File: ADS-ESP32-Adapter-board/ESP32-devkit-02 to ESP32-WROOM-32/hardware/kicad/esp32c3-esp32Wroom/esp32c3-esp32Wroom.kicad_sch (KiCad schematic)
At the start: 4 parts, among them J1 Conn_01x15_esp32_devkit_V1_el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, J2 Conn_01x15_esp32_devkit_V1_el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, J3 Conn_01x15_esp32_c3_devkit_02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, J4 Conn_01x15_esp32_c3_devkit_02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

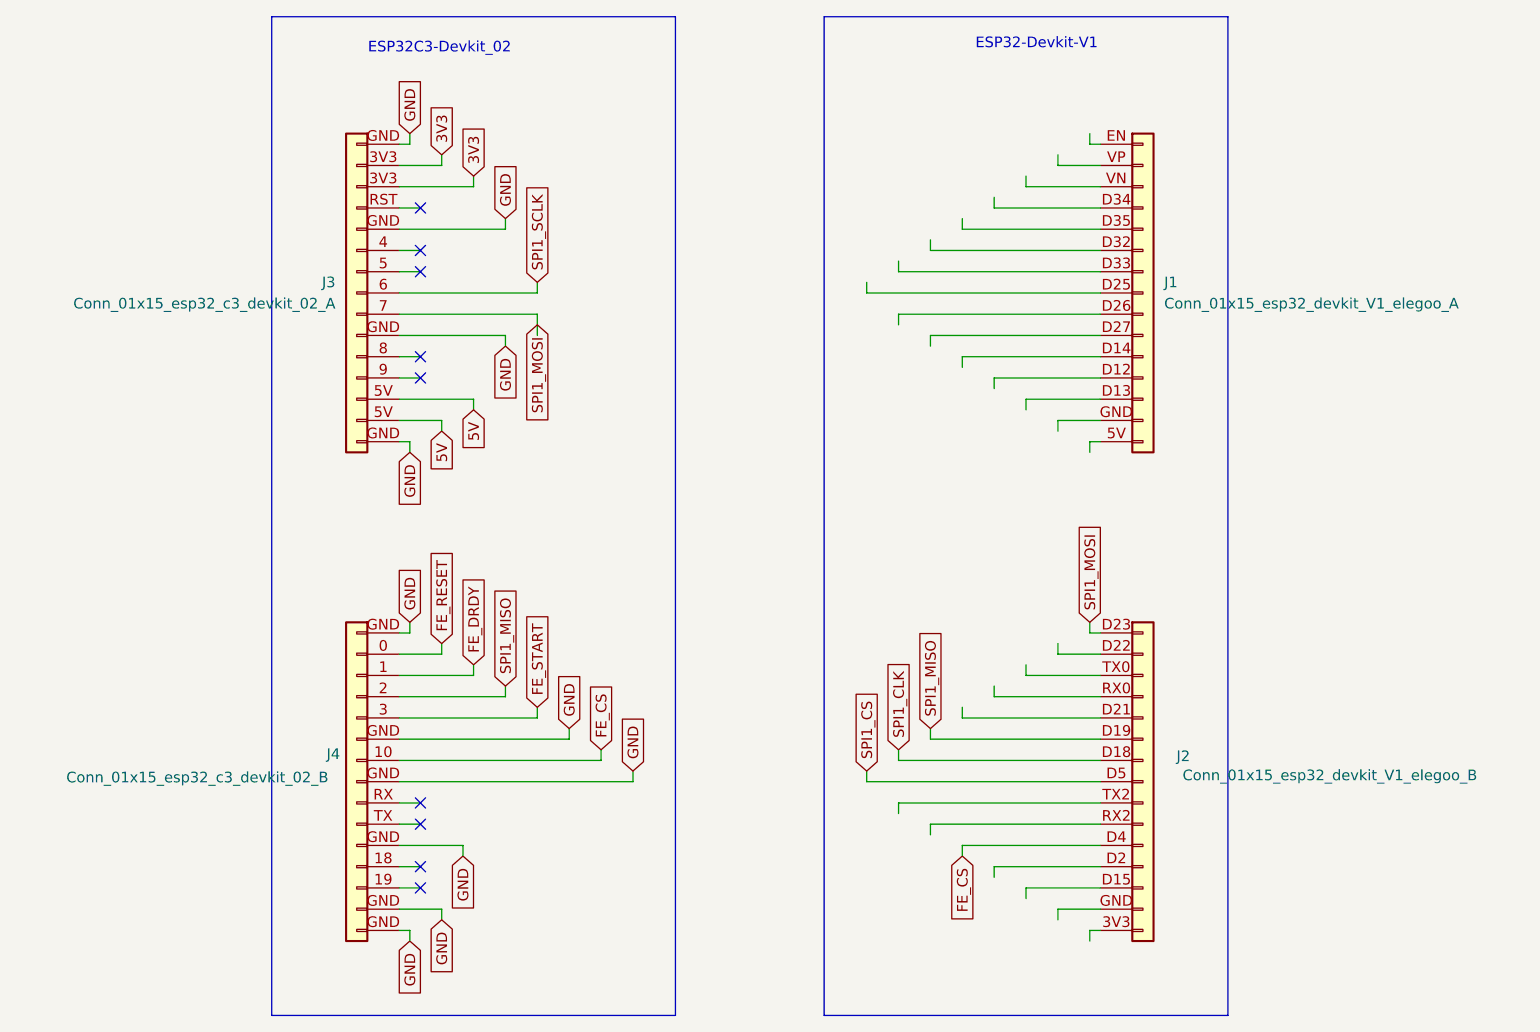
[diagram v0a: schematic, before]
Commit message: Add lock files for ESP32-WROOM-32 hardware configuration
- Created new lock files: ~esp32c3-esp32Wroom.kicad_pcb.lck and ~esp32c3-esp32Wroom.kicad_pro.lck
- Both files contain hostname and username information for the development environment.
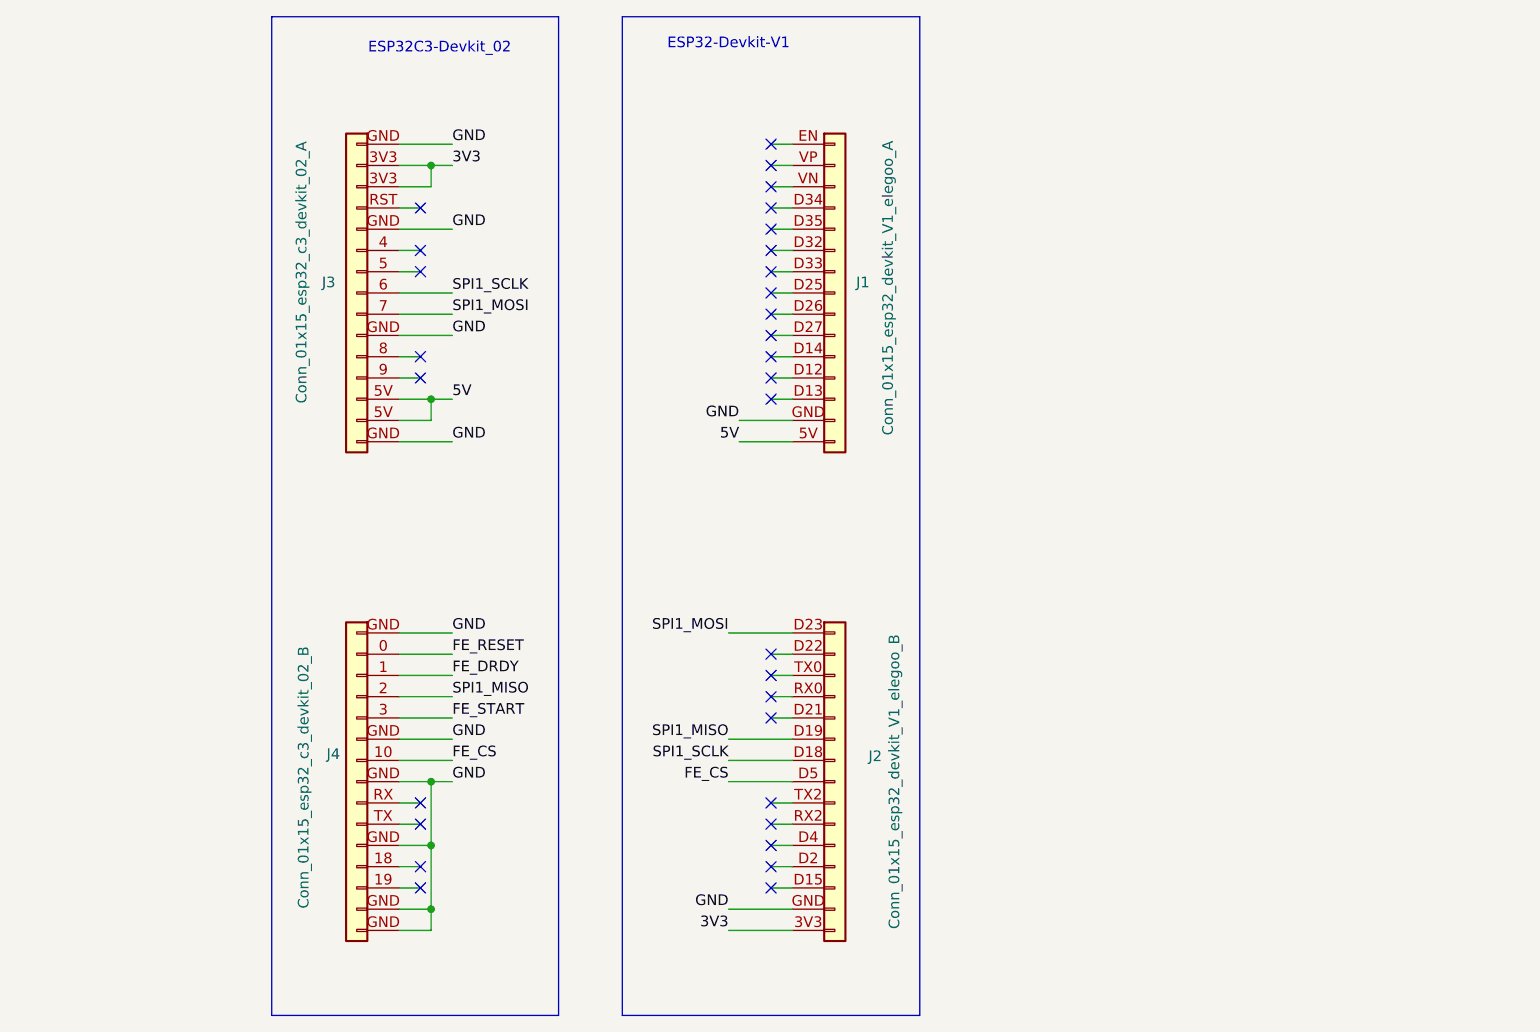
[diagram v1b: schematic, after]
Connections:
- net SPI1_CLK is gone; now on net SPI1_SCLK: J2.D18 (Pin_7)
- net SPI1_CS is gone; now on net FE_CS: J2.D5 (Pin_8)
- net 3V3: now also J2.3V3 (Pin_15)
- net 5V: now also J1.5V (Pin_15)
- net FE_CS: no longer J2.D4 (Pin_11)
- net GND: now also J1.GND (Pin_14), J2.GND (Pin_14)
- no-connect marks 9 -> 31
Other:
- moved on the sheet: J1, J2
